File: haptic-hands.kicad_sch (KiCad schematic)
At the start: 24 parts, among them M1 Motor_DC, SW1 SW_Push, SW2 SW_Push_45deg, SW3 SW_Push_45deg, SW4 SW_Push_45deg, SW5 SW_Push_45deg, SW6 SW_Push_45deg, SW7 SW_Push_45deg, SW8 SW_Push

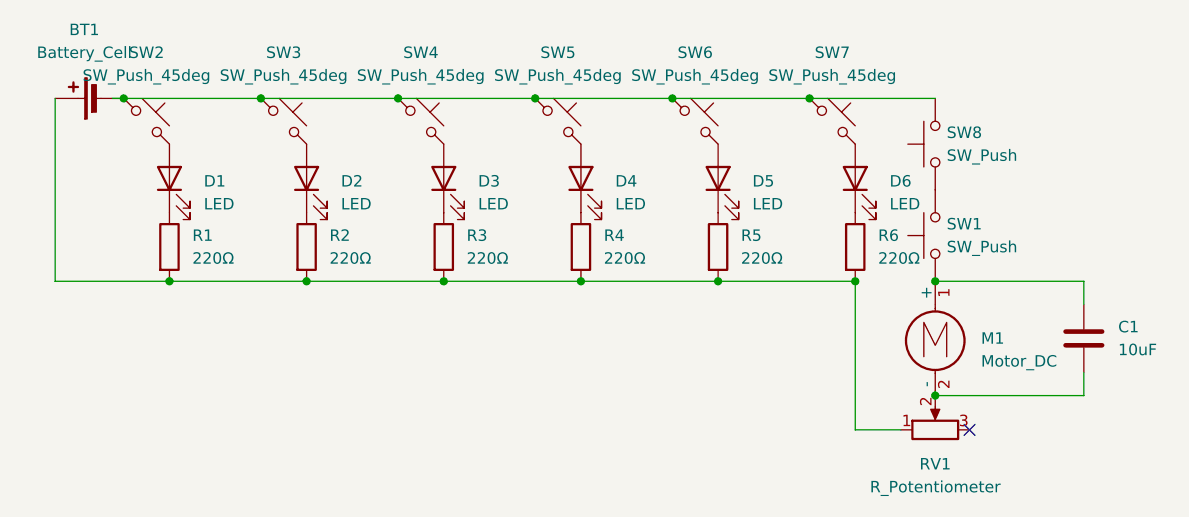
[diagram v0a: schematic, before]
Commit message: Add Haptic Hands logo
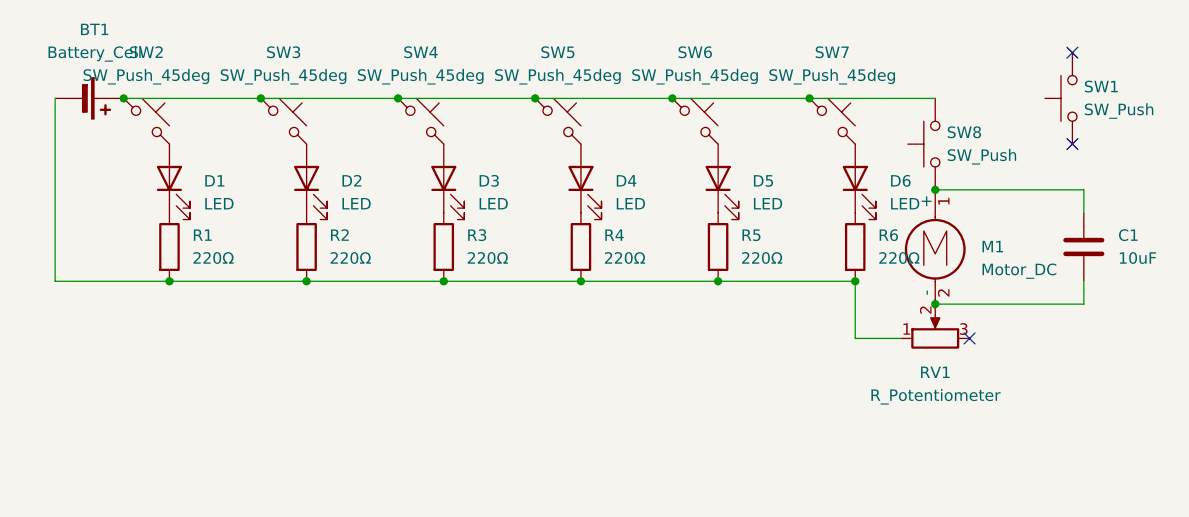
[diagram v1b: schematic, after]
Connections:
- net at R1.2, R2.2, R3.2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: now also BT1.2 (-); no longer BT1.1 (+)
- net at SW2.1, SW3.1, SW4.1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: now also BT1.1 (+); no longer BT1.2 (-)
- net at C1.1, M1.1 (+): now also SW8.1; no longer SW1.1
- net at SW1.2: no longer SW8.1
- no-connect marks 1 -> 3
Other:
- moved on the sheet: BT1, C1, M1, RV1, SW1
